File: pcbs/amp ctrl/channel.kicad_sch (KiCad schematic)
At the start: 101 parts

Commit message: Schematic file fix, misc. PCB
Fixed issue with KiCAD's automatic V5→V6 migration (corrected in 6.0.11) that caused problems with component references in multi-channel schematic sheets
Finished migration in amp ctrl PCB, inc. re-assigning "exclude from BOM" attributes to testpoints, solder jumpers
Added mounting hole to amp ctrl PCB for addl support to Ethernet jacks, power connector through stiffener
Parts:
- JP15, JP16, JP17, JP18, JP19, JP20, JP76, JP87, TP10, TP16, TP17, TP41, TP8, TP9: renamed from ?; now left out of the parts list
- gave numbers to parts that had none: 84

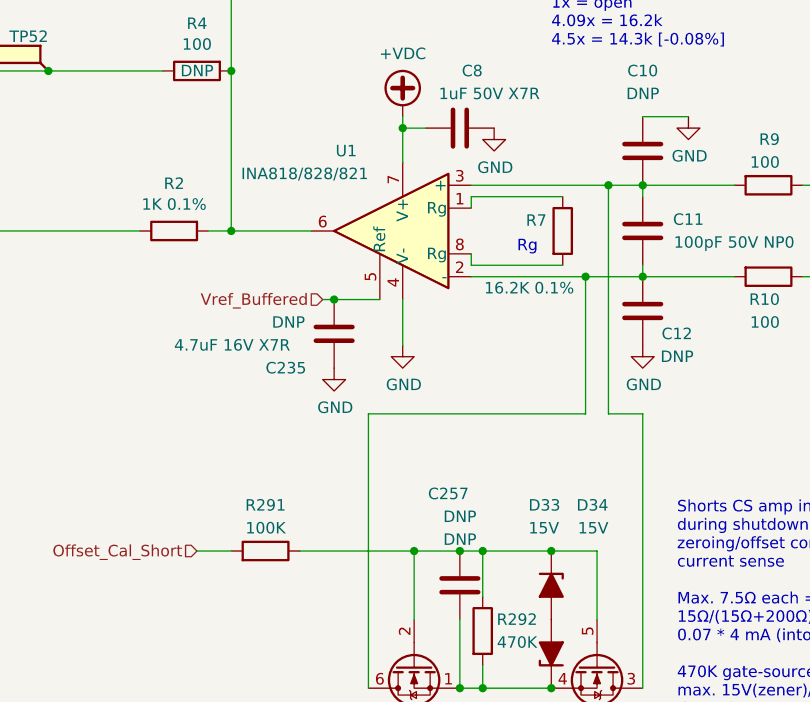
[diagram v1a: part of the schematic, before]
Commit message: New CS amp, misc. layout
Changed current sense amp from INA828 to INA821/819 due to availability: schematic, layout for channel 1 (#6)
Moved some thermistor components & ~Shutdown cap out of the way of the stiffener (#3)
Updated footprints: SOD-323F for slightly larger solderable pads, SOIC-8 to remove excessive length on inside edge
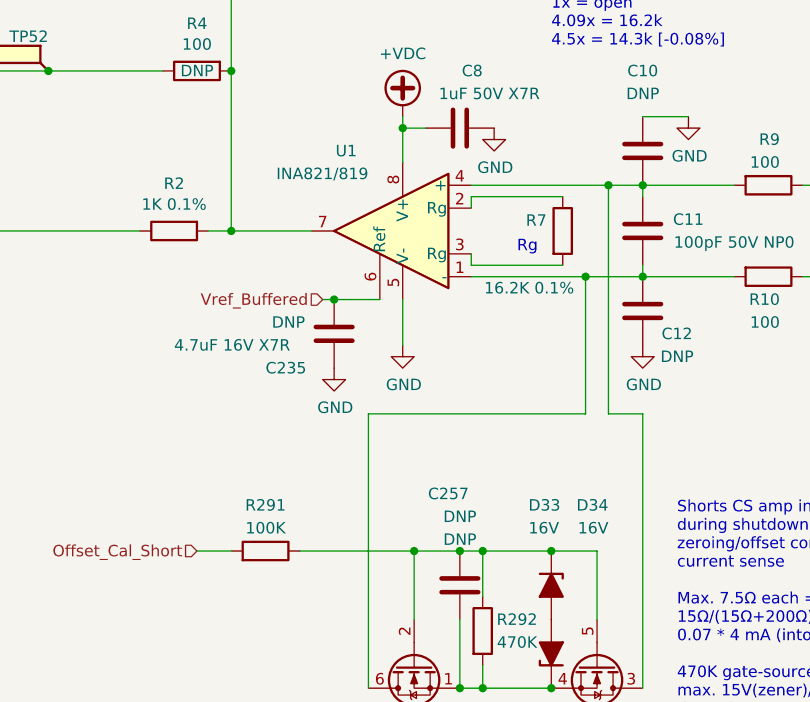
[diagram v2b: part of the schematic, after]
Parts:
- D31, D32: footprint Martinos_std:D_SOD-323F -> Don_std:D_SOD-323F
- D33, D34: value 15V -> 16V; footprint Martinos_std:D_SOD-123 -> Don_std:D_SOD-323F; Manufacturer ON Semiconductor -> Rohm Semiconductor; Manufacturer Alt. (none) -> ON Semi; Part Number MMSZ4702T1G -> UDZVTE-1716B; Part Number Alt. (none) -> MM3Z16VB
- U1: value INA818/828/821 -> INA821/819; footprint Martinos_std:SOIC-8_3.9x4.9mm_P1.27mm -> Don_std:SOIC-8_3.9x4.9mm_P1.27mm; symbol Amplifier_Instrumentation:INA128 -> Don:INA821_INA819; Part Number INA818ID -> INA821ID; Part Number Alt. INA818IDR, INA828ID, INA828IDR, INA821ID, INA821IDR -> INA821IDR, INA819ID, INA819IDR
- U2: footprint Martinos_std:SOIC-8_3.9x4.9mm_P1.27mm -> Don_std:SOIC-8_3.9x4.9mm_P1.27mm
- U73: footprint Martinos_std:SOIC-8_3.9x4.9mm_P1.27mm -> Don_std:SOIC-8_3.9x4.9mm_P1.27mm; Type (none) -> SMT
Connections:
- net +VDC: now also U1.8 (V+); no longer U1.7 (V+)
- net GND: now also U1.5 (V-); no longer U1.4 (V-)
- net Vref_Buffered: now also U1.6 (Ref); no longer U1.5 (Ref)
- net at U1.1 (-): now also C11.2, C12.1, Q37.6 (D), R10.2; no longer R7.1
- net at C10.2, C11.1, Q37.3 (D)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: now also U1.4 (+); no longer U1.3 (+)
- net at JP17.2 (B), R2.2, R4.2: now also U1.7; no longer U1.6
- net at R7.2: now also U1.3 (Rg); no longer U1.8 (Rg)
- new net: R7.1, U1.2 (Rg)
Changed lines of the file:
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@@
     (pin "2")
   )
-  (symbol (lib_id "Amplifier_Instrumentation:INA128") (at 156.21 175.26 0) (mirror y) (unit 1)
+  (symbol (lib_id "Don:INA821_INA819") (at 156.21 175.26 0) (mirror y) (unit 1)
     (in_bom yes) (on_board yes)
     (property "Reference" "U1" (id 0) (at 151.13 166.37 0)
       (effects (font (size 1.27 1.27)) (justify left))
     )
-    (property "Value" "INA818/828/821" (id 1) (at 152.4 168.91 0)
-      (effects (font (size 1.27 1.27)) (justify left))
-    )
-    (property "Footprint" "Martinos_std:SOIC-8_3.9x4.9mm_P1.27mm" (id 2) (at 153.67 175.26 0)
+    (property "Value" "INA821/819" (id 1) (at 152.4 168.91 0)
+      (effects (font (size 1.27 1.27)) (justify left))
+    )
+    (property "Footprint" "Don_std:SOIC-8_3.9x4.9mm_P1.27mm" (id 2) (at 153.67 175.26 0)
       (effects (font (size 1.27 1.27)) hide)
     )
@@
       (effects (font (size 1.27 1.27)) hide)
     )
-    (property "Part Number" "INA818ID" (id 5) (at 156.21 175.26 0)
+    (property "Part Number" "INA821ID" (id 5) (at 156.21 175.26 0)
       (effects (font (size 1.27 1.27)) hide)
     )
@@
       (effects (font (size 1.27 1.27)) hide)
     )
-    (property "Part Number Alt." "INA818IDR, INA828ID, INA828IDR, INA821ID, INA821IDR" (id 8) (at 156.21 175.26 0)
+    (property "Part Number Alt." "INA821IDR, INA819ID, INA819IDR" (id 8) (at 156.21 175.26 0)
       (effects (font (size 1.27 1.27)) hide)
     )
@@
       (effects (font (size 1.27 1.27)) (justify left))
     )
-    (property "Footprint" "Martinos_std:SOIC-8_3.9x4.9mm_P1.27mm" (id 2) (at 161.29 78.74 0)
+    (property "Footprint" "Don_std:SOIC-8_3.9x4.9mm_P1.27mm" (id 2) (at 161.29 78.74 0)
       (effects (font (size 1.27 1.27)) (justify left) hide)
     )
@@
     (property "Reference" "U73" (id 0) (at 55.88 30.48 0))
     (property "Value" "TBD" (id 1) (at 55.88 33.02 0))
-    (property "Footprint" "Martinos_std:SOIC-8_3.9x4.9mm_P1.27mm" (id 2) (at 53.34 39.37 0)
+    (property "Footprint" "Don_std:SOIC-8_3.9x4.9mm_P1.27mm" (id 2) (at 53.34 39.37 0)
       (effects (font (size 1.27 1.27)) hide)
     )
@@
     )
     (property "DNP" "DNP" (id 4) (at 55.88 35.56 0))
+    (property "Type" "SMT" (id 5) (at 53.34 39.37 0)
+      (effects (font (size 1.27 1.27)) hide)
+    )
     (pin "1")
     (pin "2")
@@
     (property "Reference" "U73" (id 0) (at 92.71 27.7622 0))
     (property "Value" "TBD" (id 1) (at 92.71 30.0736 0))
-    (property "Footprint" "Martinos_std:SOIC-8_3.9x4.9mm_P1.27mm" (id 2) (at 92.71 39.37 0)
+    (property "Footprint" "Don_std:SOIC-8_3.9x4.9mm_P1.27mm" (id 2) (at 92.71 39.37 0)
       (effects (font (size 1.27 1.27)) hide)
     )
@@
     )
     (property "DNP" "DNP" (id 4) (at 92.71 32.385 0))
+    (property "Type" "SMT" (id 5) (at 92.71 39.37 0)
+      (effects (font (size 1.27 1.27)) hide)
+    )
     (pin "1")
     (pin "2")
@@
       (effects (font (size 1.27 1.27)) (justify left))
     )
-    (property "Footprint" "Martinos_std:SOIC-8_3.9x4.9mm_P1.27mm" (id 2) (at 115.57 40.64 0)
+    (property "Footprint" "Don_std:SOIC-8_3.9x4.9mm_P1.27mm" (id 2) (at 115.57 40.64 0)
       (effects (font (size 1.27 1.27)) hide)
     )
@@
     (property "DNP" "DNP" (id 4) (at 114.5032 42.9514 0)
       (effects (font (size 1.27 1.27)) (justify left))
+    )
+    (property "Type" "SMT" (id 5) (at 115.57 40.64 0)
+      (effects (font (size 1.27 1.27)) hide)
     )
     (pin "1")
@@
       (effects (font (size 1.27 1.27)) (justify left))
     )
-    (property "Value" "15V" (id 1) (at 170.18 208.28 90)
-      (effects (font (size 1.27 1.27)) (justify left))
-    )
-    (property "Footprint" "Martinos_std:D_SOD-123" (id 2) (at 172.72 214.63 0)
+    (property "Value" "16V" (id 1) (at 170.18 208.28 90)
+      (effects (font (size 1.27 1.27)) (justify left))
+    )
+    (property "Footprint" "Don_std:D_SOD-323F" (id 2) (at 172.72 214.63 0)
       (effects (font (size 1.27 1.27)) hide)
     )
@@
       (effects (font (size 1.27 1.27)) hide)
     )
-    (property "Manufacturer" "ON Semiconductor" (id 4) (at 172.72 214.63 90)
-      (effects (font (size 1.27 1.27)) hide)
-    )
-    (property "Part Number" "MMSZ4702T1G" (id 5) (at 172.72 214.63 90)
+    (property "Manufacturer" "Rohm Semiconductor" (id 4) (at 172.72 214.63 90)
+      (effects (font (size 1.27 1.27)) hide)
+    )
+    (property "Part Number" "UDZVTE-1716B" (id 5) (at 172.72 214.63 90)
       (effects (font (size 1.27 1.27)) hide)
     )
     (property "Type" "SMT" (id 6) (at 172.72 214.63 0)
+      (effects (font (size 1.27 1.27)) hide)
+    )
+    (property "Manufacturer Alt." "ON Semi" (id 7) (at 172.72 214.63 90)
+      (effects (font (size 1.27 1.27)) hide)
+    )
+    (property "Part Number Alt." "MM3Z16VB" (id 8) (at 172.72 214.63 90)
       (effects (font (size 1.27 1.27)) hide)
     )
@@
     (property "Reference" "D32" (id 0) (at 52.07 242.57 90))
     (property "Value" "1N4448WS/BAS16J" (id 1) (at 59.69 245.11 90))
-    (property "Footprint" "Martinos_std:D_SOD-323F" (id 2) (at 48.26 243.84 0)
+    (property "Footprint" "Don_std:D_SOD-323F" (id 2) (at 48.26 243.84 0)
       (effects (font (size 1.27 1.27)) hide)
     )
@@
     (property "Reference" "D31" (id 0) (at 45.72 250.19 90))
     (property "Value" "1N4448WS/BAS16J" (id 1) (at 53.34 252.73 90))
-    (property "Footprint" "Martinos_std:D_SOD-323F" (id 2) (at 41.91 250.19 0)
+    (property "Footprint" "Don_std:D_SOD-323F" (id 2) (at 41.91 250.19 0)
       (effects (font (size 1.27 1.27)) hide)
     )
@@
       (effects (font (size 1.27 1.27)) (justify left))
     )
-    (property "Value" "15V" (id 1) (at 179.07 208.28 90)
-      (effects (font (size 1.27 1.27)) (justify left))
-    )
-    (property "Footprint" "Martinos_std:D_SOD-123" (id 2) (at 172.72 222.25 0)
+    (property "Value" "16V" (id 1) (at 179.07 208.28 90)
+      (effects (font (size 1.27 1.27)) (justify left))
+    )
+    (property "Footprint" "Don_std:D_SOD-323F" (id 2) (at 172.72 222.25 0)
       (effects (font (size 1.27 1.27)) hide)
     )
@@
       (effects (font (size 1.27 1.27)) hide)
     )
-    (property "Manufacturer" "ON Semiconductor" (id 4) (at 172.72 222.25 90)
-      (effects (font (size 1.27 1.27)) hide)
-    )
-    (property "Part Number" "MMSZ4702T1G" (id 5) (at 172.72 222.25 90)
+    (property "Manufacturer" "Rohm Semiconductor" (id 4) (at 172.72 222.25 90)
+      (effects (font (size 1.27 1.27)) hide)
+    )
+    (property "Part Number" "UDZVTE-1716B" (id 5) (at 172.72 222.25 90)
       (effects (font (size 1.27 1.27)) hide)
     )
@@
       (effects (font (size 1.27 1.27)) hide)
     )
+    (property "Manufacturer Alt." "ON Semi" (id 7) (at 172.72 222.25 90)
+      (effects (font (size 1.27 1.27)) hide)
+    )
+    (property "Part Number Alt." "MM3Z16VB" (id 8) (at 172.72 222.25 90)
+      (effects (font (size 1.27 1.27)) hide)
+    )

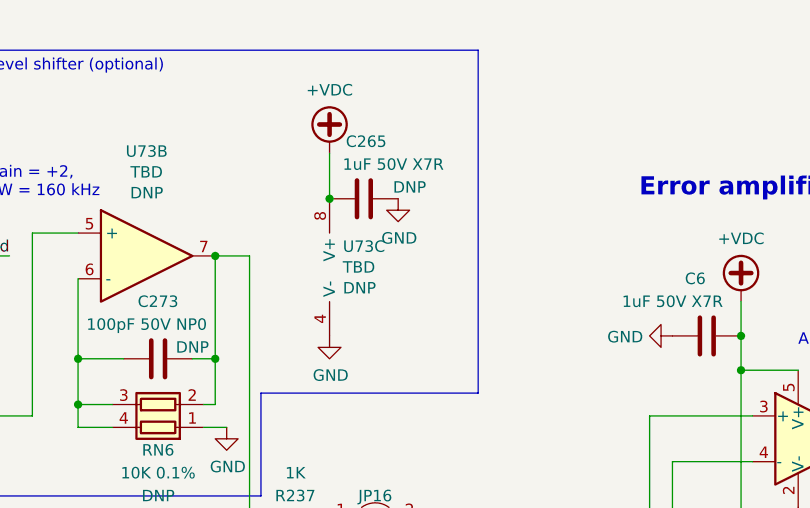
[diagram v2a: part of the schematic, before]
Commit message: DRC fixes
Deleted track stubs and overlapping vias, other misc. DRC fixes (#3)
Shrank width of SOT-563 pads to fall within 0.16 mm clearance (6.3 mils)
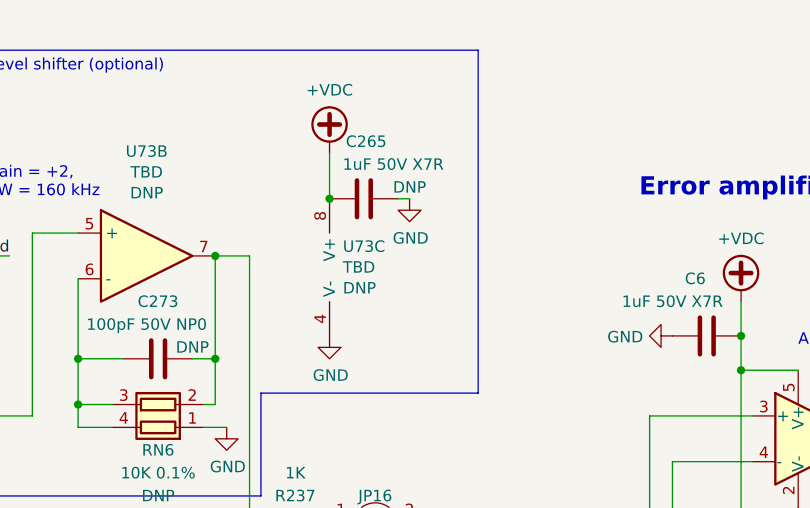
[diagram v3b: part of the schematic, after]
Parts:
- Q37: footprint Martinos_std:SOT-563 -> Don_std:SOT-563
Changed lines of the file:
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@@
     (stroke (width 0) (type default) (color 0 0 0 0))
   )
+  (wire (pts (xy 121.92 33.02) (xy 120.65 33.02))
+    (stroke (width 0) (type default) (color 0 0 0 0))
+  )
   (wire (pts (xy 294.64 158.75) (xy 298.45 158.75))
     (stroke (width 0) (type default) (color 0 0 0 0))
@@
       (effects (font (size 1.27 1.27)) (justify left))
     )
-    (property "Footprint" "Martinos_std:SOT-563" (id 2) (at 177.8 228.6 0)
+    (property "Footprint" "Don_std:SOT-563" (id 2) (at 177.8 228.6 0)
       (effects (font (size 1.27 1.27)) hide)
     )
@@
     (property "Reference" "Q37" (id 0) (at 157.48 229.8446 90))
     (property "Value" "2N7002" (id 1) (at 157.48 232.156 90))
-    (property "Footprint" "Martinos_std:SOT-563" (id 2) (at 157.48 228.6 0)
+    (property "Footprint" "Don_std:SOT-563" (id 2) (at 157.48 228.6 0)
       (effects (font (size 1.27 1.27)) hide)
     )
@@
     (pin "2")
   )
-  (symbol (lib_id "power:GND") (at 120.65 33.02 0) (unit 1)
+  (symbol (lib_id "power:GND") (at 121.92 33.02 0) (unit 1)
     (in_bom yes) (on_board yes)
-    (property "Reference" "#PWR0397" (id 0) (at 120.65 39.37 0)
+    (property "Reference" "#PWR0397" (id 0) (at 121.92 39.37 0)
       (effects (font (size 1.27 1.27)) hide)
     )
-    (property "Value" "GND" (id 1) (at 120.777 37.4142 0))
-    (property "Footprint" "" (id 2) (at 120.65 33.02 0)
+    (property "Value" "GND" (id 1) (at 122.047 37.4142 0))
+    (property "Footprint" "" (id 2) (at 121.92 33.02 0)
       (effects (font (size 1.27 1.27)) hide)
     )
-    (property "Datasheet" "" (id 3) (at 120.65 33.02 0)
+    (property "Datasheet" "" (id 3) (at 121.92 33.02 0)
       (effects (font (size 1.27 1.27)) hide)
     )

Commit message: Manufacturing fixes for amp control board
Arranged *.Fab text for assembly drawings
Minor stiffener outline fixes, silkscreen fixes
Fixed missing BOM fields on some parts
Removed exported manufacturing files from version control
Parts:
- D31, D32: Type (none) -> SMT
- RN5, RN6: footprint Resistor_SMD:R_Array_Convex_2x0606 -> Don_std:R_Array_Convex_2x0606
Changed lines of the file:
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@@
   (title_block
     (title "Output Channel")
-    (rev "D3")
+    (date "2023-05-04")
+    (rev "D4")
     (company "Martinos Center @ MGH")
     (comment 1 "Don Straney")
@@
       (effects (font (size 1.27 1.27)) (justify right))
     )
-    (property "Footprint" "Resistor_SMD:R_Array_Convex_2x0606" (id 2) (at 56.515 52.07 90)
+    (property "Footprint" "Don_std:R_Array_Convex_2x0606" (id 2) (at 56.515 52.07 90)
       (effects (font (size 1.27 1.27)) hide)
     )
@@
     (property "Reference" "RN6" (id 0) (at 93.98 60.96 90))
     (property "Value" "10K 0.1%" (id 1) (at 93.98 63.5 90))
-    (property "Footprint" "Resistor_SMD:R_Array_Convex_2x0606" (id 2) (at 93.98 51.435 90)
+    (property "Footprint" "Don_std:R_Array_Convex_2x0606" (id 2) (at 93.98 51.435 90)
       (effects (font (size 1.27 1.27)) hide)
     )
@@
       (effects (font (size 1.27 1.27)) hide)
     )
+    (property "Type" "SMT" (id 8) (at 48.26 243.84 90)
+      (effects (font (size 1.27 1.27)) hide)
+    )
     (pin "1")
     (pin "2")
@@
     )
     (property "DNP" "DNP" (id 8) (at 44.45 247.65 90))
+    (property "Type" "SMT" (id 9) (at 41.91 250.19 90)
+      (effects (font (size 1.27 1.27)) hide)
+    )
     (pin "1")
     (pin "2")

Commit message: Misc. mfg
Marked top-side testpoints on amp control board as DNP
Updated serial interface board's BOM-placement-help file
Exported stiffener file for amp control board
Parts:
- R58: Part Number RK73H2ATTDD4700F -> RK73H2ATTD4700F
- TP18, TP2, TP20, TP52: DNP (none) -> DNP
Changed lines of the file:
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@@
+      (effects (font (size 1.27 1.27)) hide)
+    )
+    (property "DNP" "DNP" (id 7) (at 93.98 76.2 0)
       (effects (font (size 1.27 1.27)) hide)
     )
@@
       (effects (font (size 1.27 1.27)) hide)
     )
+    (property "DNP" "DNP" (id 7) (at 405.13 213.36 0)
+      (effects (font (size 1.27 1.27)) hide)
+    )
     (pin "1")
   )
@@
       (effects (font (size 1.27 1.27)) hide)
     )
+    (property "DNP" "DNP" (id 7) (at 405.13 226.06 0)
+      (effects (font (size 1.27 1.27)) hide)
+    )
     (pin "1")
   )
@@
     )
     (property "Part Number" "5019" (id 6) (at 116.84 157.48 0)
+      (effects (font (size 1.27 1.27)) hide)
+    )
+    (property "DNP" "DNP" (id 7) (at 116.84 157.48 0)
       (effects (font (size 1.27 1.27)) hide)
     )
@@
       (effects (font (size 1.27 1.27)) hide)
     )
-    (property "Part Number" "RK73H2ATTDD4700F" (id 6) (at 41.91 224.79 0)
-      (effects (font (size 1.27 1.27)) hide)
-    )
+    (property "Part Number" "RK73H2ATTD4700F" (id 6) (at 41.91 224.79 0)
+      (effects (font (size 1.27 1.27)) hide)
+    )

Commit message: Upgraded to KiCAD 7.0 format Added 10µF cap to ADC's REFP pins to fix the voltage reference output (#15) Corrected ADC & DAC reset by adding a separate reset circuit (#14) Increased Cfbk compensation cap on each channel to work out-of-the-box with small coils (#16)
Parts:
- C9: value 20pF 50V NP0 -> 82pF 50V NP0; Part Number C0603C200J5GACTU -> C0603C820J5GACTU
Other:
- note added: "Gain = 1+(49.4K/Rg) 1x = open 4.05x = 16.2k 4.5x = 14.3k [-0.08%]"
- note removed: "5A = 0Ω 4A = 4.02KΩ 3A = 10KΩ 2.5A = 14.7KΩ 1A = 57.6KΩ"
- note removed: "Cut jumpers to set <5A current limit by soldering resistors across the jumpers Only meant for unusual/extreme cases though as hitting the current limit causes severe oscillation in the OPA548 output stages!"
- note removed: "Gain = 1+(50K/Rg) 1x = open 4.09x = 16.2k 4.5x = 14.3k [-0.08%]"
- note removed: "Holds the OPA548 outputs @ approx. +VDC/2 when in shutdown; this requires sourcing ~4 mA into each OPA548 output (8 mA total) This ensures that the CS amp has a valid common-mode input voltage, so that its offset + ADC offset can be measured during shutdown to calibrate out the offset in the system Optionally, can hold the error amp output to ~ +VDC/2 as well, if its power is gated by the ~Shutdo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"
- note removed: "OPA548 output currents cause a few mV of voltage drop on the ground plane from the left to the right side of the board, causing 10 mA+ errors in the ADC readings when multiple channels are driving currents >1A. Slot in ground plane keeps the setpoint (SP-In), Vref, and current sense (CS) signals separate; the error amp sees the few mV of ground sag as common-mode voltage and can reject it"
- note removed: "Shorts CS amp inputs together during shutdown, to allow zeroing/offset correction for current sense Max. 7.5Ω each = 15Ω total 15Ω/(15Ω+200Ω) = 0.07x divider when enabled 0.07 * 4 mA (into disabled OPA548 outputs) = 0.28 mA sensed 470K gate-source pulldown means that max. 15V(zener)/470K = 0.032 mA is forced through MOSFETs by pulldown...although this current is shared equally between both MOSFET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"
- note removed: "Trim resistor notes: 0.05% matching in resistor networks produces up to 5.6 mA offset when using ext. analog input and level shifter (2.5Vref * 0.05% * 2 / 0.45 V/A = 5.6 mA) but if desired, a series trim resistor can be added to cancel the offset: use 1-4.7Ω"

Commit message: Amp ctrl: lengthened ADC & DAC reset delay to ~50 ms (#14) Backplane: added clock multiplier for 10 Mhz scanner clock (fixes #21) Backplane: reduced R5 from 10 to 1 ohm, to avoid excessive voltage drop (#20) Backplane: replaced 15V regulator with efficient voltage limiter (#20) Backplane: changed all mounting holes to signal ground Backplane: replaced +2.5V regulator with a higher-current model to support FPGA I/O bank current draw Updated to KiCAD 8
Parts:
- C10, C12, C19, C257, C5, C7, D5, R14, R3, R5: now not fitted
- R292: Part Number RK73H2ATTE4703F -> RK73H2ATTD4703F
